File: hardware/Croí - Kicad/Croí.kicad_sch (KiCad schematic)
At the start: 38 parts, among them J1 JTAG-10 PIN, J2 XT30PW-M, J3 ESQ-110-14-G-D, Q1 IPP060N06N, U1 W25Q128JVS, U2 ADXL375BCCZ, U3 STM32F072C8Tx, U4 BME680, U5 BMP390, U7 TLV70433DBVT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

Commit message: minor changes
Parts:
- added C13: 100nF, Capacitor_SMD:C_0402_1005Metric, symbol Device:C
- added C27, C28: 8pF, Capacitor_SMD:C_0402_1005Metric, symbol Device:C
- added R1: 10KΩ, Resistor_SMD:R_0402_1005Metric, symbol Device:R
- added XTAL1: NX3225GD-8MHZ-STD-CRA-3, XTAL_NX3225GD-8MHZ-STD-CRA-3_NDK, symbol STDCRA38M:NX3225GD-8MHZ-STD-CRA-3
- R6, R7: value 60 Ω -> 60Ω
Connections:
- net GND: now also C13.2, C27.1, C28.2, R1.2
- net NRST: now also J3.17, C13.1; no longer J3.10
- net at U3.44 (BOOT0): now also R1.1
- net at U3.5 (PF0): now also C27.2, XTAL1.1
- net at U3.6 (PF1): now also C28.1, XTAL1.2
- net Mode_sel: no longer names the net of U3.26 (PB13)
- net SWCLK renamed SWCLK2
- net SWCLK2: now also J3.10; no longer J3.17
- no-connect marks 44 -> 41
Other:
- moved on the sheet: C11, C22, C24, C25, C26, C5, C9, D2, R6, R7, U1, U8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

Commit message: random ass changes
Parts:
- added J4: 436500303, MOLEX_436500303, symbol 436500303:436500303
- added U6: ~, Library:Untitled, symbol l:_1
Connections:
- net 3.3V: now also J4.1, U6. (unimportant)
- net GND: now also J4.2, J4.S1 (SHIELD1), J4.S2 (SHIELD2), U6. (unimportant)
- new net: J4.3, U6. (unimportant)
- no-connect marks 41 -> 43

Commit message: Crazy new changes
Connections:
- net 3.3V: now also U6.1 (3.3V); no longer U6. (unimportant)
- net GND: now also U6.2 (GND), U6.4 (GND); no longer U6. (unimportant)
- net at J4.3: now also U6.5 (Video); no longer U6. (unimportant)
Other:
- moved on the sheet: C1, C10, C12, C13, C15, C17, C2, C27, C28, C3, C4, C6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

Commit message: cleaned up
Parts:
- removed J4: 436500303, MOLEX_436500303, symbol 436500303:436500303
- removed U6: ~, Library:Untitled, symbol l:_1
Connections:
- no-connect marks 43 -> 41

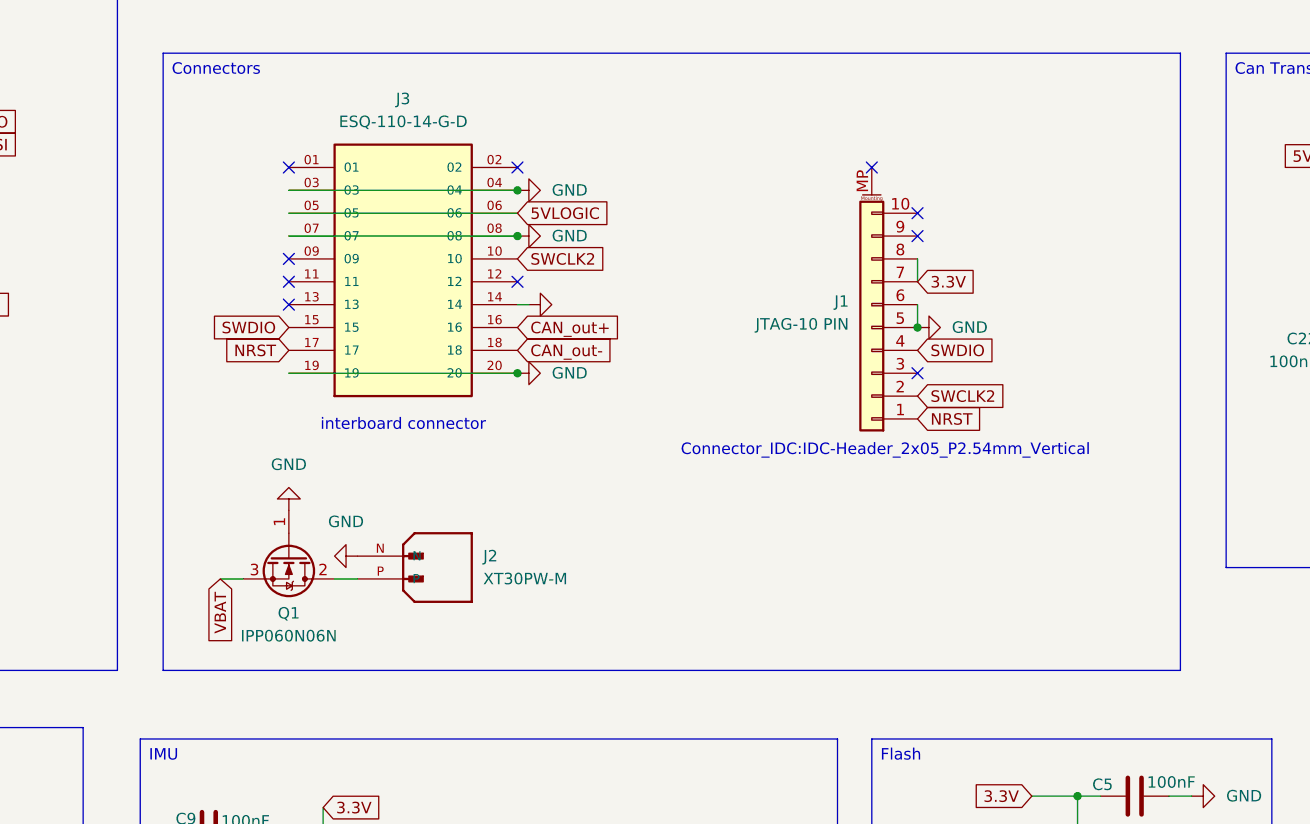
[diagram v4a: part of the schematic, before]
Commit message: Started Applying Global Changes
1. Shape and screwholes
2. Mosfet
3. New Molex
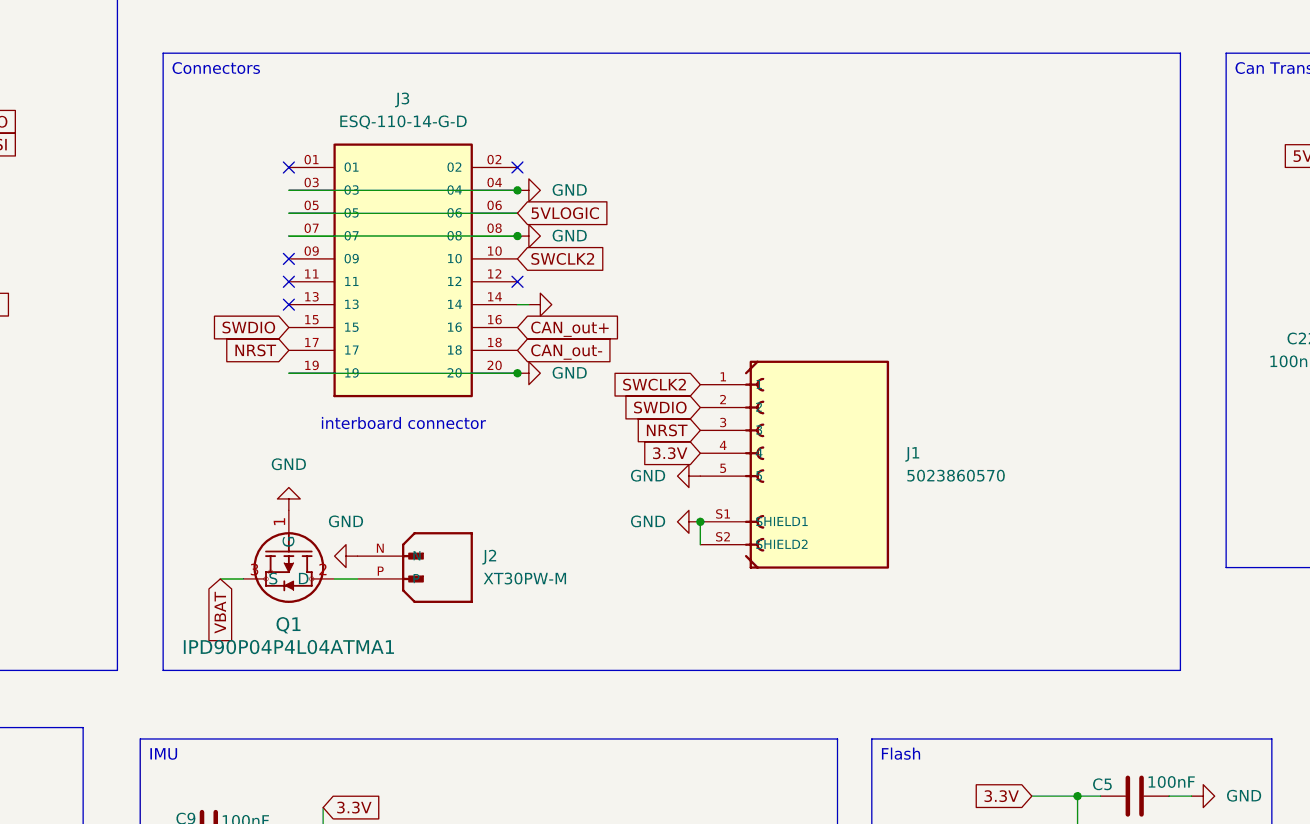
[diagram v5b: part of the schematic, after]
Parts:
- removed J1: JTAG-10 PIN, Connector_IDC:IDC-Header_2x05_P2.54mm_Vertical, symbol Connector_Generic_MountingPin:Conn_01x10_MountingPin
- removed Q1: IPP060N06N, Package_TO_SOT_THT:TO-220-3_Vertical, symbol Transistor_FET:IPP060N06N
- added J1: 5023860570, 5023860570:MOLEX_5023860570, symbol 5023860570:5023860570
- added Q1: IPD90P04P4L04ATMA1, PG-TO252-3-313_INF, symbol l:IPD90P04P4L04ATMA1
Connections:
- net 3.3V: now also J1.4
- net GND: now also J1.5, J1.S1 (SHIELD1), J1.S2 (SHIELD2), Q1.1 (G)
- net NRST: now also J1.3
- net SWCLK2: now also J1.1
- net SWDIO: now also J1.2
- net VBAT: now also Q1.3 (S)
- net at J2.P: now also Q1.2 (D)
- no-connect marks 41 -> 37
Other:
- note removed: "Connector_IDC:IDC-Header_2x05_P2.54mm_Vertical"

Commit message: Only missing one thing off the notion i believe, all 3d modlels should work
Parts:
- J1: footprint 5023860570:MOLEX_5023860570 -> MOLEX:MOLEX_5023860570
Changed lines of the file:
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@@
 			)
 		)
-		(property "Footprint" "5023860570:MOLEX_5023860570"
+		(property "Footprint" "MOLEX:MOLEX_5023860570"
 			(at 215.9 113.03 0)
 			(effects

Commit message: lots left to do, but good enough for render
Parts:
- removed C21: 100nF, Capacitor_SMD:C_0402_1005Metric, symbol Device:C
- removed C23: 1 uF, Capacitor_SMD:C_0402_1005Metric, symbol Device:C
- removed U7: TLV70433DBVT, footprints:DBV0005A_M, symbol TLV70433DBVT:TLV70433DBVT
- added 3v3, C+1, C-1, GND1: S2761-46R, HARWIN_S2761-46R, symbol S2761-46R:S2761-46R
- added D1: BAT54C, Package_TO_SOT_SMD:SOT-23, symbol Diode:BAT54C
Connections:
- net 3.3V: now also 3v3.1
- net CAN_out+: now also C+1.1
- net CAN_out-: now also C-1.1
- net GND: now also GND1.1
- new net 5V_LOGIC: D1.2
- new net VBAT_Local: D1.1
- new net power/vin: D1.3
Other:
- added sheet power (power.kicad_sch)

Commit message: running
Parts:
- removed J2: XT30PW-M, footprints:AMASS_XT30PW-M, symbol XT30PW-M:XT30PW-M
- added 5VL1: S2761-46R, HARWIN_S2761-46R, symbol S2761-46R:S2761-46R
- added J2: 39-29-1048, MOLEX_39-29-1048, symbol 39-29-1048:39-29-1048
- renumbered 3v3 to 3V3, C+1 to CAN+1, C-1 to CAN-1
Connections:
- net 5VLOGIC: now also J3.11, J3.12, 5VL1.1; no longer J3.05, J3.06
- net GND: now also J3.01, J3.02, J3.09, J3.10, J3.13, J3.15, J3.17, J2.3, J2.4; no longer J3.03, J3.04, J3.07, J3.08
- net NRST: no longer J3.17
- net SWCLK2: no longer J1.1, J3.10
- net SWDIO: no longer J3.15
- net at Q1.2 (D): now also J2.1, J2.2
- new net: J3.03, J3.04, J3.05, J3.06, J3.07, J3.08
- new net SWCLK: J1.1
- no-connect marks 37 -> 32
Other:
- moved on the sheet: C11, C5, C9, J1, Q1, U1, U9
